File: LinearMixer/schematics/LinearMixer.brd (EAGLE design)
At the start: 50.3 x 99.4 mm, 61 parts, among them IC1 QUAD_OPAMPD, IC2 QUAD_OPAMPD, X1 53048-05, X2 53048-05, X3 53048-03, X4 53048-03, X5 53048-03

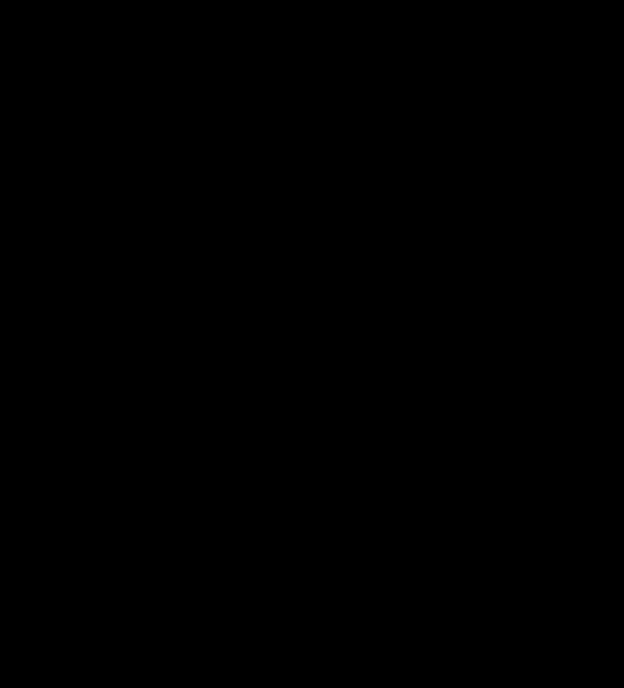
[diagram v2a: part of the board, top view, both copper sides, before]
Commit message: added pull-downs on inputs
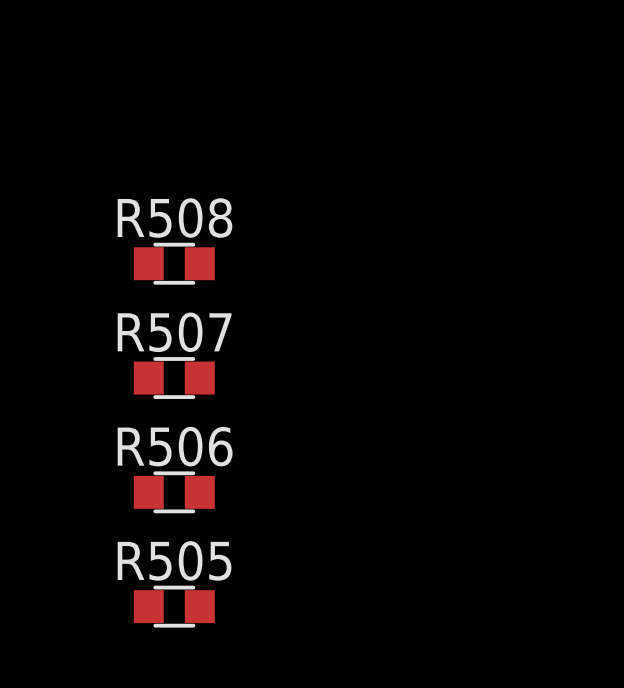
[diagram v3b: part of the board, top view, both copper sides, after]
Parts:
- added R505, R506, R507, R508: 100k, resistor:R0603
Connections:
- net GND: now also R505.2, R506.2, R507.2, R508.2
- net IN_1: now also R505.1
- net IN_2: now also R506.1
- net IN_3: now also R507.1
- net IN_4: now also R508.1
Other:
- board text added: "LinearMixer Rev02"
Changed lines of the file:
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@@
 <dimension x1="1.524" y1="0" x2="51.816" y2="0" x3="26.67" y3="-4.445" textsize="1.778" layer="47"/>
 <text x="4.445" y="64.135" size="1.778" layer="47" font="vector" rot="R90">Rebel Technology</text>
-<text x="6.985" y="64.135" size="1.778" layer="47" font="vector" rot="R90">LinearMixer Rev01</text>
+<text x="6.985" y="64.135" size="1.778" layer="47" font="vector" rot="R90">LinearMixer Rev02</text>
 <text x="13.97" y="85.725" size="1.778" layer="47" font="vector" rot="MR180">Rebel Technology</text>
 <text x="12.7" y="82.55" size="1.778" layer="47" font="vector" rot="MR180">LinearMixer Rev01</text>
@@
 <attribute name="VALUE" x="24.045" y="95.185" size="1.27" layer="27"/>
 </element>
+<element name="R508" library="resistor" package="R0603" value="100k" x="-5.08" y="-9.525"/>
+<element name="R507" library="resistor" package="R0603" value="100k" x="-5.08" y="-13.335"/>
+<element name="R506" library="resistor" package="R0603" value="100k" x="-5.08" y="-17.145"/>
+<element name="R505" library="resistor" package="R0603" value="100k" x="-5.08" y="-20.955"/>
 </elements>
 <signals>
@@
 <via x="31.115" y="45.085" extent="1-16" drill="0.6"/>
 <contactref element="X5" pad="2"/>
+<contactref element="R505" pad="2"/>
+<contactref element="R506" pad="2"/>
+<contactref element="R507" pad="2"/>
+<contactref element="R508" pad="2"/>
+<wire x1="34.87" y1="96.52" x2="43.87" y2="96.52" width="0" layer="19" extent="1-1"/>
+<wire x1="36.87" y1="89.02" x2="34.87" y2="96.52" width="0" layer="19" extent="1-1"/>
+<wire x1="29.845" y1="90.17" x2="36.87" y2="89.02" width="0" layer="19" extent="1-1"/>
+<wire x1="24.52" y1="94.615" x2="28.82" y2="90.17" width="0" layer="19" extent="1-1"/>
+<wire x1="26.67" y1="97.81" x2="24.52" y2="94.615" width="0" layer="19" extent="1-1"/>
+<wire x1="18.47" y1="96.52" x2="23.495" y2="94.615" width="0" layer="19" extent="1-1"/>
+<wire x1="24.47" y1="85.725" x2="28.82" y2="90.17" width="0" layer="19" extent="1-1"/>
+<wire x1="28.87" y1="80.01" x2="24.47" y2="85.725" width="0" layer="19" extent="1-1"/>
+<wire x1="34.87" y1="77.47" x2="33.655" y2="80.01" width="0" layer="19" extent="1-1"/>
+<wire x1="28.36" y1="76.2" x2="28.87" y2="80.01" width="0" layer="19" extent="1-1"/>
+<wire x1="26.035" y1="76.2" x2="27.305" y2="76.2" width="0" layer="19" extent="1-1"/>
+<wire x1="18.47" y1="77.47" x2="24.98" y2="76.2" width="0" layer="19" extent="1-1"/>
+<wire x1="36.87" y1="69.97" x2="34.87" y2="77.47" width="0" layer="19" extent="1-1"/>
+<wire x1="43.87" y1="77.47" x2="34.87" y2="77.47" width="0" layer="19" extent="1-1"/>
+<wire x1="9.47" y1="96.52" x2="18.47" y2="96.52" width="0" layer="19" extent="1-1"/>
+<wire x1="11.47" y1="89.02" x2="9.47" y2="96.52" width="0" layer="19" extent="1-1"/>
+<wire x1="9.47" y1="77.47" x2="18.47" y2="77.47" width="0" layer="19" extent="1-1"/>
+<wire x1="11.47" y1="69.97" x2="9.47" y2="77.47" width="0" layer="19" extent="1-1"/>
+<wire x1="34.87" y1="58.42" x2="36.87" y2="69.97" width="0" layer="19" extent="1-1"/>
+<wire x1="28.36" y1="58.42" x2="34.87" y2="58.42" width="0" layer="19" extent="1-1"/>
+<wire x1="26.035" y1="58.42" x2="27.305" y2="58.42" width="0" layer="19" extent="1-1"/>
+<wire x1="18.47" y1="58.42" x2="24.98" y2="58.42" width="0" layer="19" extent="1-1"/>
+<wire x1="36.87" y1="50.92" x2="34.87" y2="58.42" width="0" layer="19" extent="1-1"/>
+<wire x1="32.0675" y1="47.625" x2="36.87" y2="50.92" width="0" layer="19" extent="1-1"/>
+<wire x1="29.27" y1="45.085" x2="29.27" y2="47.625" width="0" layer="19" extent="1-1"/>
+<wire x1="24.07" y1="47.625" x2="29.27" y2="47.625" width="0" layer="19" extent="1-1"/>
+<wire x1="24.07" y1="45.085" x2="24.07" y2="47.625" width="0" layer="19" extent="1-1"/>
+<wire x1="18.47" y1="39.37" x2="21.2725" y2="45.085" width="0" layer="19" extent="1-1"/>
+<wire x1="34.87" y1="39.37" x2="31.115" y2="45.085" width="0" layer="19" extent="1-1"/>
+<wire x1="36.87" y1="31.87" x2="34.87" y2="39.37" width="0" layer="19" extent="1-1"/>
+<wire x1="45.74" y1="31.75" x2="36.87" y2="31.87" width="0" layer="19" extent="1-1"/>
+<wire x1="43.87" y1="39.37" x2="45.74" y2="31.75" width="0" layer="19" extent="1-1"/>
+<wire x1="45.74" y1="46.99" x2="43.87" y2="39.37" width="0" layer="19" extent="1-1"/>
+<wire x1="46.99" y1="55.88" x2="45.74" y2="46.99" width="0" layer="19" extent="1-1"/>
+<wire x1="49.53" y1="55.88" x2="46.99" y2="55.88" width="0" layer="19" extent="1-1"/>
+<wire x1="49.53" y1="58.42" x2="49.53" y2="55.88" width="0" layer="19" extent="1-1"/>
+<wire x1="49.53" y1="60.96" x2="49.53" y2="58.42" width="0" layer="19" extent="1-1"/>
+<wire x1="46.99" y1="60.96" x2="49.53" y2="60.96" width="0" layer="19" extent="1-1"/>
+<wire x1="46.99" y1="58.42" x2="46.99" y2="55.88" width="0" layer="19" extent="1-1"/>
+<wire x1="43.87" y1="58.42" x2="46.99" y2="58.42" width="0" layer="19" extent="1-1"/>
+<wire x1="9.47" y1="58.42" x2="18.47" y2="58.42" width="0" layer="19" extent="1-1"/>
+<wire x1="11.47" y1="50.92" x2="9.47" y2="58.42" width="0" layer="19" extent="1-1"/>
+<wire x1="8.235" y1="46.99" x2="11.47" y2="50.92" width="0" layer="19" extent="1-1"/>
+<wire x1="9.47" y1="39.37" x2="8.235" y2="46.99" width="0" layer="19" extent="1-1"/>
+<wire x1="5.295" y1="36.83" x2="9.47" y2="39.37" width="0" layer="19" extent="1-1"/>
+<wire x1="8.235" y1="31.75" x2="5.3975" y2="35.56" width="0" layer="19" extent="1-1"/>
+<wire x1="11.47" y1="31.87" x2="8.235" y2="31.75" width="0" layer="19" extent="1-1"/>
+<wire x1="37.72" y1="20.32" x2="36.87" y2="31.87" width="0" layer="19" extent="1-1"/>
+<wire x1="41.02" y1="20.32" x2="37.72" y2="20.32" width="0" layer="19" extent="1-1"/>
+<wire x1="50.42" y1="20.32" x2="41.02" y2="20.32" width="0" layer="19" extent="1-1"/>
+<wire x1="28.32" y1="20.32" x2="37.72" y2="20.32" width="0" layer="19" extent="1-1"/>
+<wire x1="25.02" y1="20.32" x2="28.32" y2="20.32" width="0" layer="19" extent="1-1"/>
+<wire x1="15.62" y1="20.32" x2="25.02" y2="20.32" width="0" layer="19" extent="1-1"/>
+<wire x1="12.32" y1="20.32" x2="15.62" y2="20.32" width="0" layer="19" extent="1-1"/>
+<wire x1="2.92" y1="20.32" x2="12.32" y2="20.32" width="0" layer="19" extent="1-1"/>
+<wire x1="50.42" y1="7.62" x2="50.42" y2="20.32" width="0" layer="19" extent="1-1"/>
+<wire x1="41.02" y1="7.62" x2="50.42" y2="7.62" width="0" layer="19" extent="1-1"/>
+<wire x1="37.72" y1="7.62" x2="41.02" y2="7.62" width="0" layer="19" extent="1-1"/>
+<wire x1="28.32" y1="7.62" x2="37.72" y2="7.62" width="0" layer="19" extent="1-1"/>
+<wire x1="25.02" y1="7.62" x2="28.32" y2="7.62" width="0" layer="19" extent="1-1"/>
+<wire x1="15.62" y1="7.62" x2="25.02" y2="7.62" width="0" layer="19" extent="1-1"/>
+<wire x1="12.32" y1="7.62" x2="15.62" y2="7.62" width="0" layer="19" extent="1-1"/>
+<wire x1="2.92" y1="7.62" x2="12.32" y2="7.62" width="0" layer="19" extent="1-1"/>
+<wire x1="-4.23" y1="-9.525" x2="2.92" y2="7.62" width="0" layer="19" extent="1-1"/>
+<wire x1="-4.23" y1="-13.335" x2="-4.23" y2="-9.525" width="0" layer="19" extent="1-1"/>
+<wire x1="-4.23" y1="-17.145" x2="-4.23" y2="-13.335" width="0" layer="19" extent="1-1"/>
+<wire x1="-4.23" y1="-20.955" x2="-4.23" y2="-17.145" width="0" layer="19" extent="1-1"/>
 </signal>
 <signal name="N$1">
@@
 <wire x1="43.18" y1="23.495" x2="43.18" y2="27.305" width="0.6096" layer="16"/>
 <wire x1="43.18" y1="27.305" x2="45.085" y2="29.21" width="0.6096" layer="16"/>
+<contactref element="R505" pad="1"/>
+<wire x1="8.255" y1="14.605" x2="-5.93" y2="-20.955" width="0" layer="19" extent="1-1"/>
 </signal>
 <signal name="N$34">
@@
 <wire x1="41.91" y1="35.56" x2="44.43" y2="35.56" width="0.6096" layer="1"/>
 <wire x1="44.43" y1="35.56" x2="45.74" y2="34.25" width="0.6096" layer="1"/>
+<contactref element="R508" pad="1"/>
+<wire x1="-5.93" y1="-9.525" x2="45.72" y2="25.22" width="0" layer="19" extent="1-1"/>
 </signal>
 <signal name="IN_3">
@@
 <wire x1="31.75" y1="41.275" x2="31.75" y2="34.29" width="0.4064" layer="16"/>
 <wire x1="31.75" y1="34.29" x2="33.02" y2="33.02" width="0.4064" layer="16"/>
+<contactref element="R507" pad="1"/>
+<wire x1="-5.93" y1="-13.335" x2="33.02" y2="25.22" width="0" layer="19" extent="1-1"/>
 </signal>
 <signal name="IN_2">
@@
 <wire x1="34.29" y1="33.655" x2="34.29" y2="30.5" width="0.4064" layer="16"/>
 <via x="34.29" y="30.5" extent="1-16" drill="0.6"/>
+<contactref element="R506" pad="1"/>
+<wire x1="-5.93" y1="-17.145" x2="20.32" y2="25.22" width="0" layer="19" extent="1-1"/>
 </signal>
 <signal name="IN_SW_4">

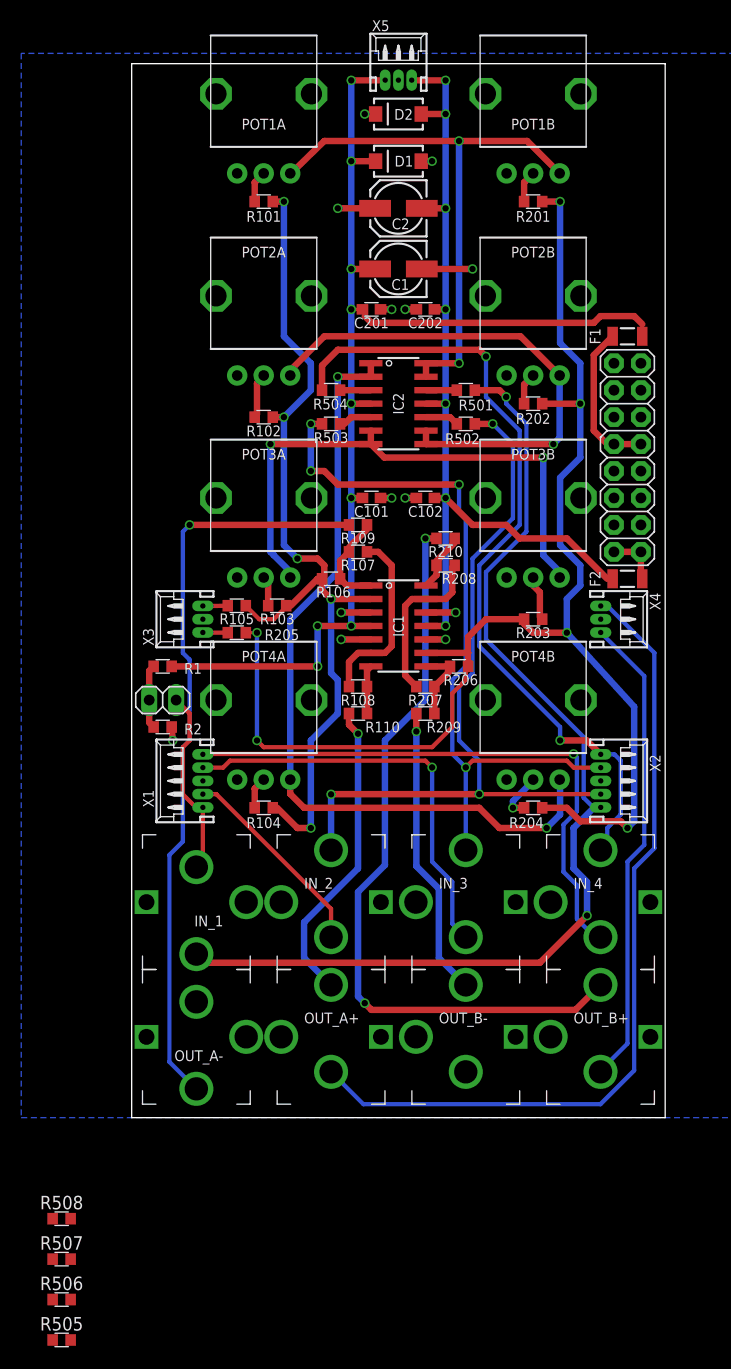
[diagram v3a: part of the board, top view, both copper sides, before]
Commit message: changed to thonkiconn jacks, turned input connectors around, rerouted
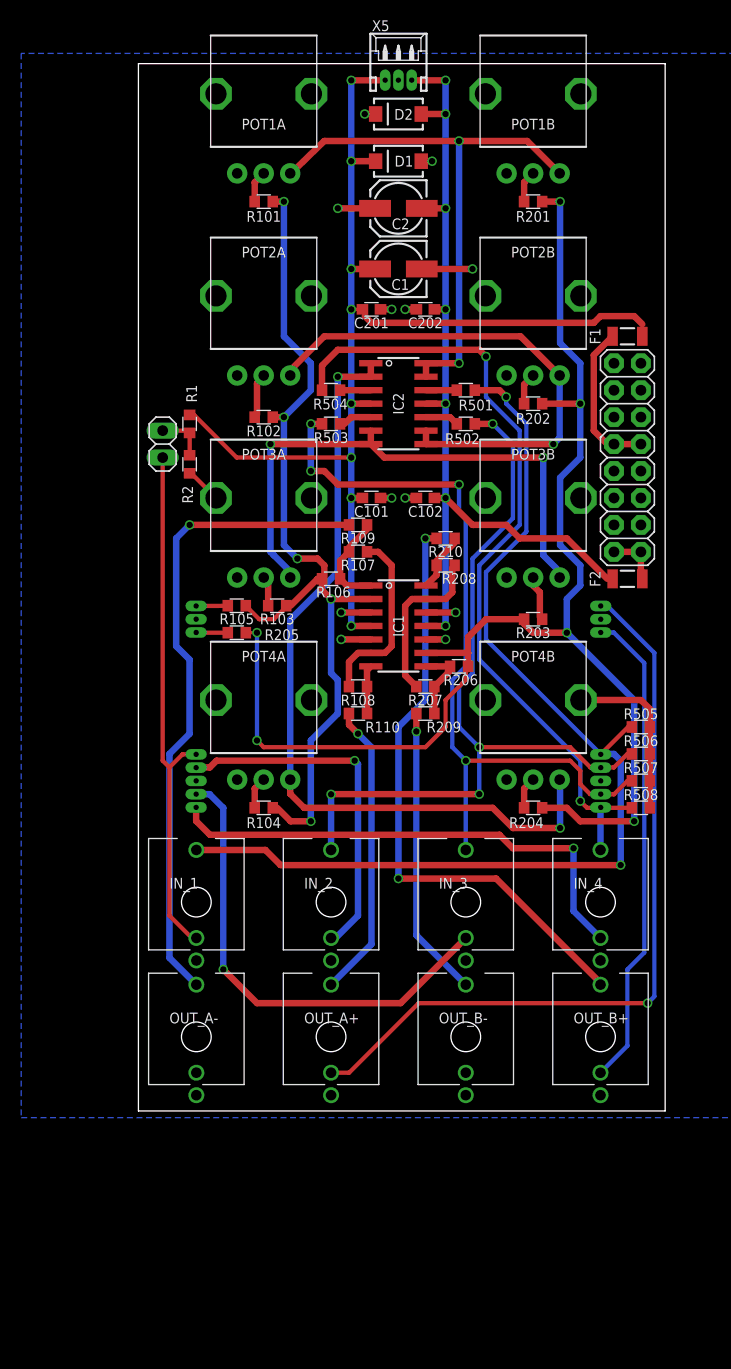
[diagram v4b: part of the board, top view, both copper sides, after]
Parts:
- removed X3: 53048-03, con-molex:53048-03
- added X6: 53048-03, con-molex:53048-03
- IN_1, IN_2, IN_3, IN_4, OUT_A+, OUT_A-, OUT_B+, OUT_B-: value JACK-PJ-301B -> THONKICONN; device Rebel:PJ-301B -> Rebel:THONKICONN
- moved R505 79.5 mm to (49.5, 36.8)
- moved R506 75.0 mm to (49.5, 34.3)
- moved R507 70.8 mm to (49.5, 31.8)
- moved R508 67.0 mm to (49.5, 29.2)
- moved R2 24.9 mm to (6.99, 61.6), turned to 270 degrees
- moved JP1 24.1 mm to (4.45, 63.5), turned to 270 degrees
- moved R1 23.0 mm to (6.99, 65.4), turned to 270 degrees
- moved X1 0.64 mm to (6.35, 31.8), flipped to the bottom, turned to 270 degrees
- turned IN_1 to 0 degrees
- turned OUT_A- to 0 degrees
- flipped X2 to the bottom, turned to 90 degrees
- flipped X7 to the bottom, turned to 90 degrees
- renumbered X4 to X7
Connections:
- net GND: now also IN_1.P$1, IN_2.P$1, IN_3.P$1, IN_4.P$1, OUT_A+.P$1, OUT_A-.P$1, OUT_B+.P$1, OUT_B-.P$1, X6.2; no longer IN_1.SHL, IN_1.SLV, IN_2.SHL, IN_2.SLV, IN_3.SHL, IN_3.SLV, IN_4.SHL, IN_4.SLV, OUT_A+.SHL, OUT_A+.SLV, OUT_A-.SHL, OUT_A-.SLV, OUT_B+.SHL, OUT_B+.SLV, OUT_B-.SHL, OUT_B-.SLV, X3.2
- net IN_1: now also IN_1.P$3; no longer IN_1.TIP
- net IN_2: now also IN_2.P$3; no longer IN_2.TIP
- net IN_3: now also IN_3.P$3; no longer IN_3.TIP
- net IN_4: now also IN_4.P$3; no longer IN_4.TIP
- net IN_A: now also X6.3; no longer X3.1
- net IN_B: now also X6.1; no longer X3.3
- net IN_SW_1: now also IN_1.P$2; no longer IN_1.SW
- net IN_SW_2: now also IN_2.P$2; no longer IN_2.SW
- net IN_SW_3: now also IN_3.P$2; no longer IN_3.SW
- net IN_SW_4: now also IN_4.P$2; no longer IN_4.SW
- net N$11: now also OUT_A-.P$3; no longer OUT_A-.TIP
- net N$15: now also OUT_B+.P$3; no longer OUT_B+.TIP
- net N$17: now also OUT_B-.P$3; no longer OUT_B-.TIP
- net N$9: now also OUT_A+.P$3; no longer OUT_A+.TIP
- net OUT_SW_A: now also OUT_A+.P$2, X7.1; no longer OUT_A+.SW, X7.3
- net OUT_SW_B: now also OUT_B+.P$2, X7.3; no longer OUT_B+.SW, X7.1
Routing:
- net IN_SW_1: track 18.0 -> 49.9 mm
- net GND: track 26.1 -> 44.4 mm, vias 13 -> 12
- net IN_SW_2: track 19.2 -> 33.4 mm, vias 0 -> 1
- net N$15: track 71.2 -> 57.5 mm
- net N$11: track 70.6 -> 61.3 mm
- net IN_SW_4: track 54.6 -> 47.4 mm
- net IN_SW_3: track 39.5 -> 45.1 mm
- net OUT_SW_A: track 78.2 -> 72.8 mm, vias 0 -> 1
- net IN_3: track 69.0 -> 74.0 mm
- net IN_2: track 71.0 -> 75.2 mm, vias 3 -> 4
- net +12V: track 114.6 -> 110.8 mm, vias 9 -> 8
- net N$44: track 4.50 -> 3.01 mm, vias 1 -> 0
- net N$7: track 6.06 -> 4.74 mm
- net N$9: track 29.1 -> 28.0 mm
- net N$52: track 85.3 -> 84.4 mm
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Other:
- board size 50.3 x 99.4 mm -> 49.7 x 98.7 mm
- board text removed: "LinearMixer Rev01"
